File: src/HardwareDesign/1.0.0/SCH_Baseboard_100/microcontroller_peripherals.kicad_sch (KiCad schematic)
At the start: 32 parts, among them IC1 RP2354B, IC2 W25Q128JVPIQ, IC3 AT24C256C-XHL-T, J1 Conn_ARM_SWD_TagConnect_TC2030, SW1 TPS645-5NC60, SW2 TPS645-5NC60, X1 12MHz 10pF

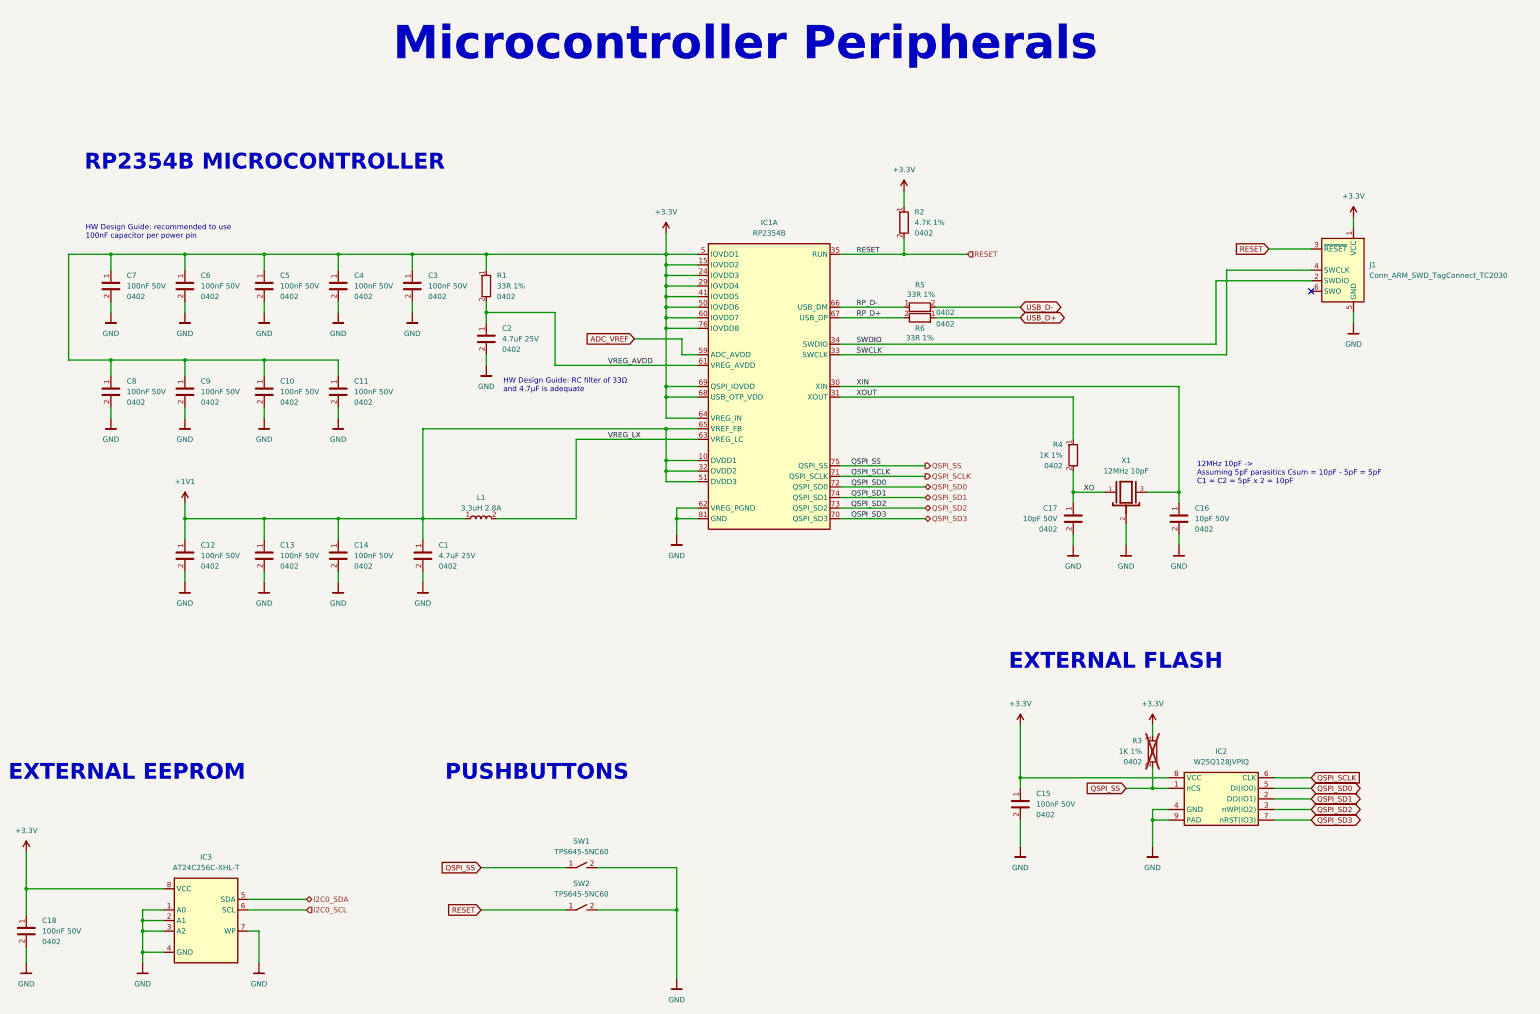
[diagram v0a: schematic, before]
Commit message: Add bladecore to design
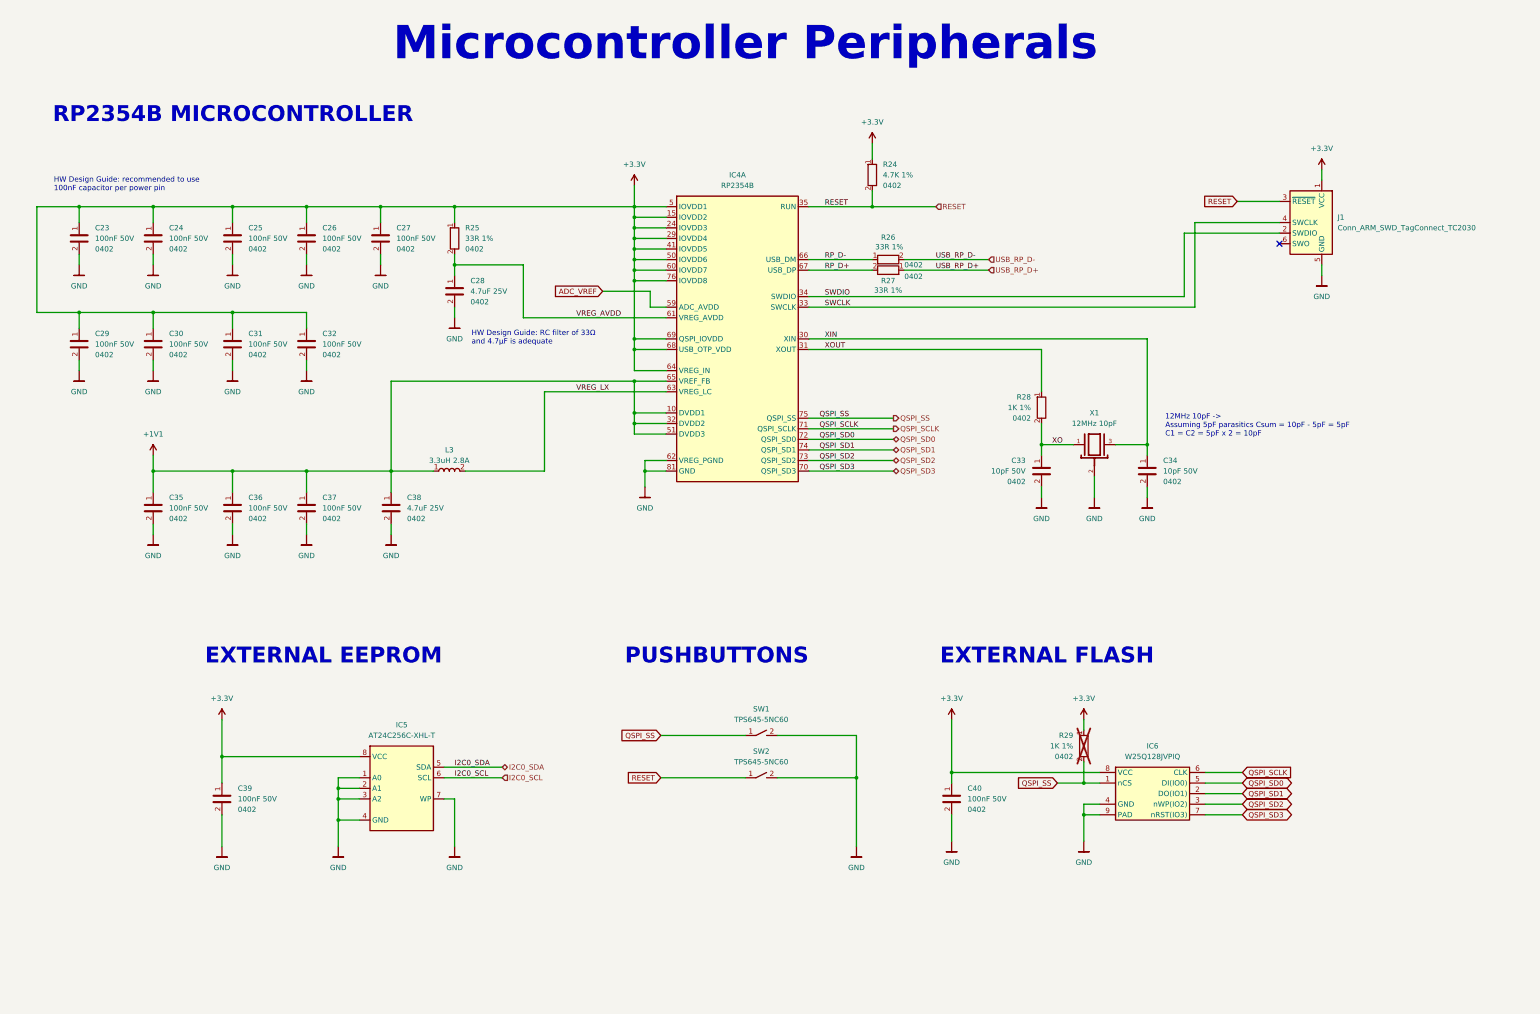
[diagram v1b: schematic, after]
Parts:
- J1: footprint Connector_PinHeader_1.27mm:PinHeader_2x07_P1.27mm_Vertical_SMD -> Connector:Tag-Connect_TC2030-IDC-FP_2x03_P1.27mm_Vertical
- renumbered C7 to C23, C6 to C24, C5 to C25, C4 to C26, C3 to C27, C2 to C28, C8 to C29, C9 to C30, C10 to C31, C11 to C32, C17 to C33, C16 to C34, C12 to C35, C13 to C36, C14 to C37, C1 to C38, C18 to C39, C15 to C40, IC1 to IC4, IC3 to IC5, IC2 to IC6, L1 to L3, R2 to R24, R1 to R25, R5 to R26, R6 to R27, R4 to R28, R3 to R29
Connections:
- net USB_D+ renamed USB_RP_D+
- net USB_D- renamed USB_RP_D-
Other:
- moved on the sheet: C23, C24, C25, C26, C27, C28, C29, C30, C31, C32, C33, C34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
